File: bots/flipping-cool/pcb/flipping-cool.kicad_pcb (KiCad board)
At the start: 2 copper layers, 90 x 70 mm, 71 parts, among them J1 XT30_BATTERY_IN_GNB4502S80AHV, J10 MATEK_ELRS_R24_P6_PWM, J11 R24_P6_VBAT_TELEMETRY_SENSE, J2 REMOVABLE_LINK_OR_RATED_SWITCH, J20 WEKA_POWER_INPUT_XT30, J21 WEKA_PWM_INPUTS_NAMED, J22 WEKA_MOTOR_OUTPUT_SOLDER_PADS, J23 MOTOR_FRONT_LEFT_POLOLU_3064, J24 MOTOR_REAR_LEFT_POLOLU_3064, J25 MOTOR_FRONT_RIGHT_POLOLU_3064, J26 MOTOR_REAR_RIGHT_POLOLU_3064, J3 VISIBLE_POWER_LED_CURRENT_LIM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, J30 SAVOX_SH0255MGP_FRONT_REAR_AX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, J31 SAVOX_SH0255MGP_LEFT_RIGHT_AX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, J32 SPARE_SERVO_PWM5, J33 SPARE_SERVO_PWM6, J4 2S_BALANCE_SENSE_NO_CHARGE, J40 SPARE_SWITCHED_VBAT_OUT_FUSED, J41 SPARE_6V_ACCESSORY, J42 OPTIONAL_CRSF_UART_PADS, J43 PWM_SPARE_BREAKOUT, J44 PIT_DEBUG_POWER_COMMS, J45 OPTIONAL_POLOLU_D24V5F3_3V3, J46 FUTURE_MCU_POWER_COMMS, J47 FUTURE_MCU_PWM_I2C_TAPS, J48 FUTURE_MCU_ADC_LED, J49 I2C_SENSOR_STEMMA_QT_QWIIC, J5 POLOLU_D36V50F6_6V_5P5A_BEC, J50 COMMON_ANODE_RGB_STATUS_LED

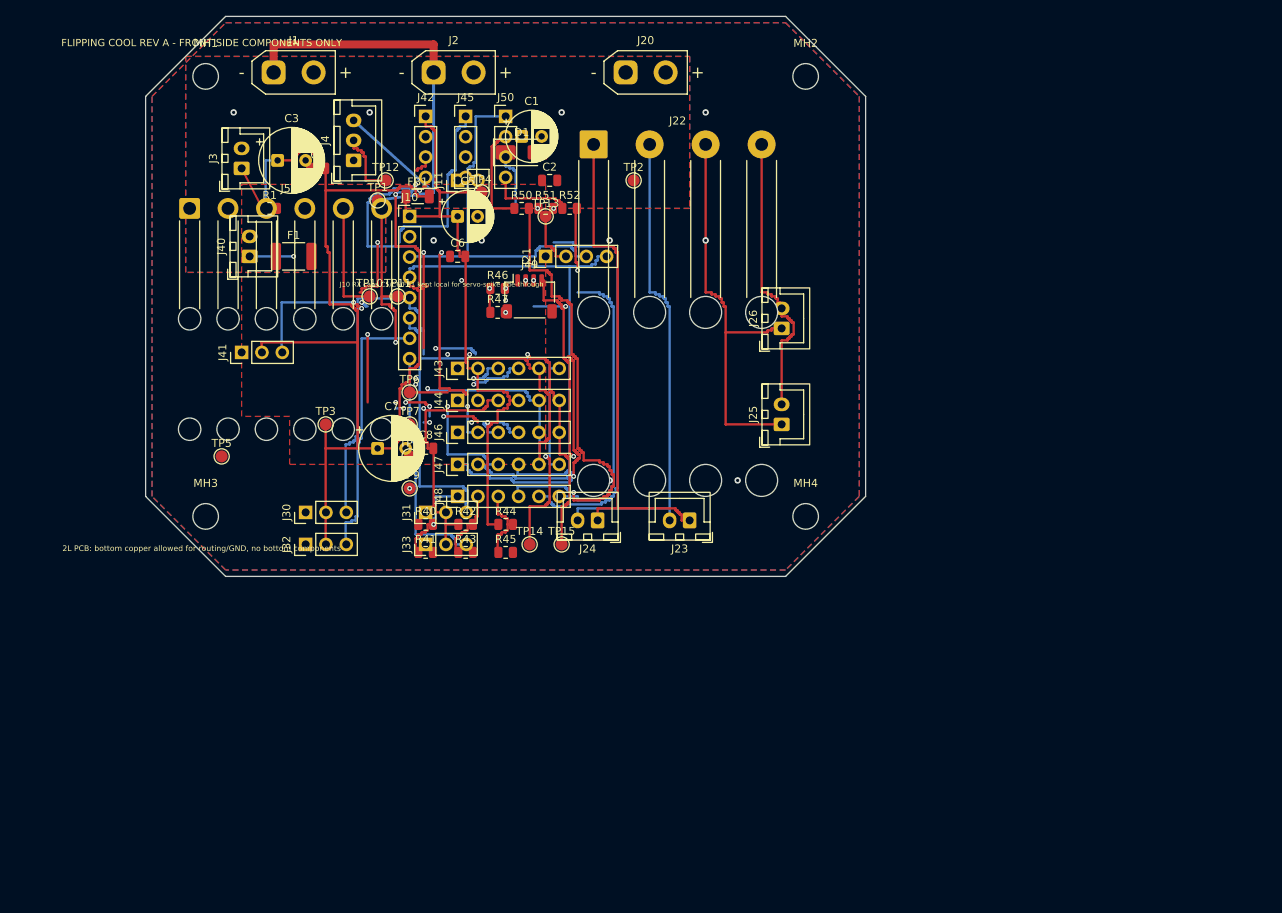
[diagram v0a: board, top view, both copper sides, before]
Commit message: Refactor KiCad PCB design by reorganizing net connections, adding a new mounting hole footprint, and updating existing footprints for resistors and test points. Adjust design rules in the project configuration, including hole clearance and via dimensions, to enhance layout precision and flexibility.
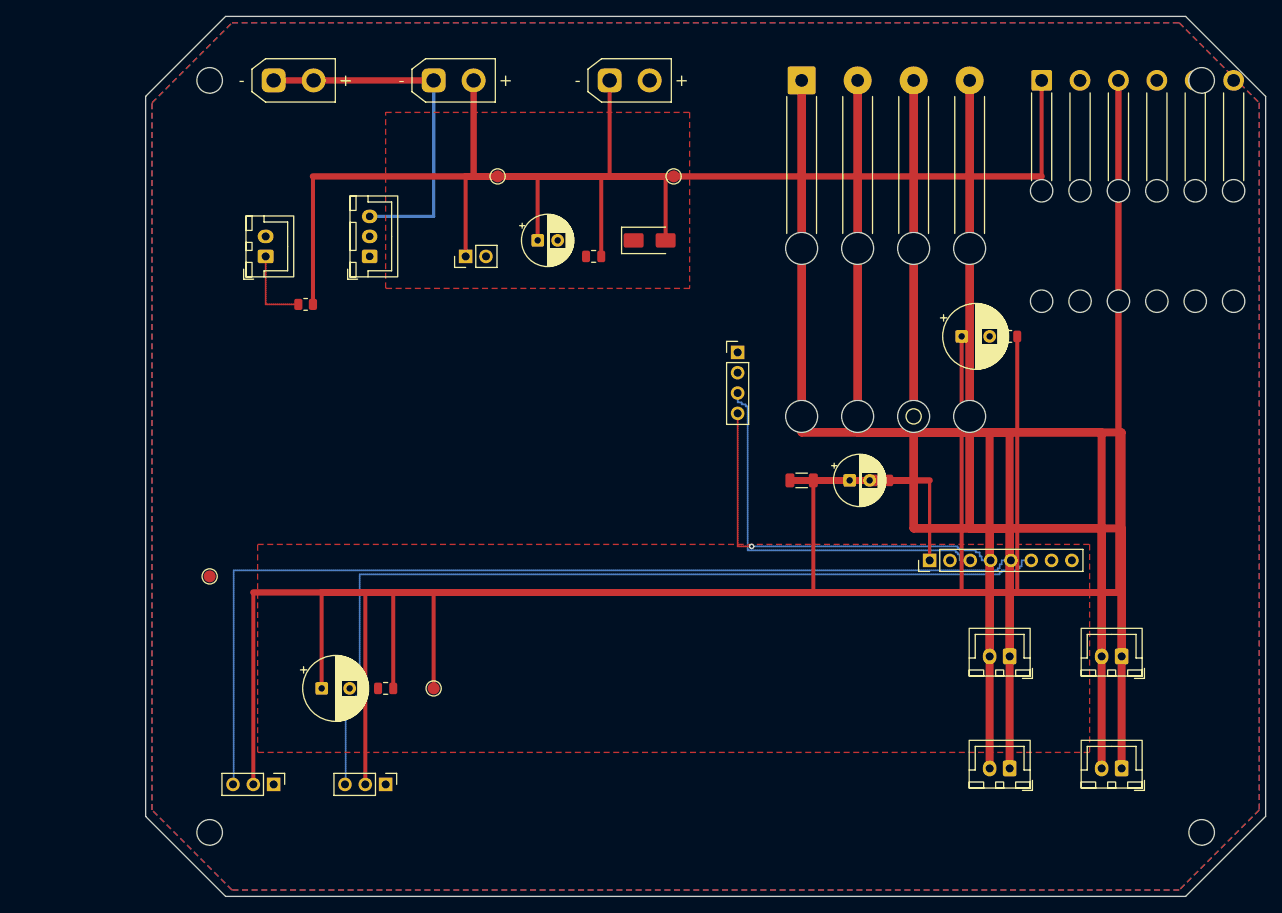
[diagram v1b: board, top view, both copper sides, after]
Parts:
- removed F1: MF-MSMF050_500mA_PTC, Fuse_1812_4532Metric_Pad1.30x3.40mm_HandSolder
- removed J32: SPARE_SERVO_PWM5, PinHeader_1x03_P2.54mm_Vertical
- removed J33: SPARE_SERVO_PWM6, PinHeader_1x03_P2.54mm_Vertical
- removed J40: SPARE_SWITCHED_VBAT_OUT_FUSED, JST_XH_B2B-XH-A_1x02_P2.50mm_Vertical
- removed J41: SPARE_6V_ACCESSORY, PinHeader_1x03_P2.54mm_Vertical
- removed J42: OPTIONAL_CRSF_UART_PADS, PinHeader_1x04_P2.54mm_Vertical
- removed J43: PWM_SPARE_BREAKOUT, PinHeader_1x06_P2.54mm_Vertical
- removed J44: PIT_DEBUG_POWER_COMMS, PinHeader_1x06_P2.54mm_Vertical
- removed J45: OPTIONAL_POLOLU_D24V5F3_3V3, PinHeader_1x04_P2.54mm_Vertical
- removed J46: FUTURE_MCU_POWER_COMMS, PinHeader_1x06_P2.54mm_Vertical
- removed J47: FUTURE_MCU_PWM_I2C_TAPS, PinHeader_1x06_P2.54mm_Vertical
- removed J48: FUTURE_MCU_ADC_LED, PinHeader_1x06_P2.54mm_Vertical
- removed J49: I2C_SENSOR_STEMMA_QT_QWIIC, JST_SH_SM04B-SRSS-TB_1x04-1MP_P1.00mm_Horizontal
- removed J50: COMMON_ANODE_RGB_STATUS_LED, PinHeader_1x04_P2.54mm_Vertical
- removed R40: 100k_ADC_VBAT_HI, R_0805_2012Metric
- removed R41: 47k_ADC_VBAT_LO, R_0805_2012Metric
- removed R42: 100k_ADC_SERVO_HI, R_0805_2012Metric
- removed R43: 47k_ADC_SERVO_LO, R_0805_2012Metric
- removed R44: 100k_ADC_RX_HI, R_0805_2012Metric
- removed R45: 47k_ADC_RX_LO, R_0805_2012Metric
- removed R46: 4k7_DNP_I2C_SDA_PULLUP, R_0805_2012Metric
- removed R47: 4k7_DNP_I2C_SCL_PULLUP, R_0805_2012Metric
- removed R50: 330R_STATUS_RED, R_0805_2012Metric
- removed R51: 330R_STATUS_GREEN, R_0805_2012Metric
- removed R52: 330R_STATUS_BLUE, R_0805_2012Metric
- removed TP10: BEC_EN_TP, TestPoint_Pad_D1.5mm
- removed TP11: BEC_PG_TP, TestPoint_Pad_D1.5mm
- removed TP12: CELL1_SENSE_TP, TestPoint_Pad_D1.5mm
- removed TP13: WEKA_5V_NC_TP, TestPoint_Pad_D1.5mm
- removed TP14: CRSF_TX_TP, TestPoint_Pad_D1.5mm
- removed TP15: CRSF_RX_TP, TestPoint_Pad_D1.5mm
- removed TP6: PWM_DRIVE_LEFT_TP, TestPoint_Pad_D1.5mm
- removed TP7: PWM_DRIVE_RIGHT_TP, TestPoint_Pad_D1.5mm
- removed TP8: PWM_WEAPON_FR_TP, TestPoint_Pad_D1.5mm
- removed TP9: PWM_WEAPON_LR_TP, TestPoint_Pad_D1.5mm
- moved J5 107.7 mm to (112.0, 8.00)
- moved C4 89.0 mm to (108.0, 40.0)
- moved C3 88.3 mm to (102.0, 40.0)
- moved J10 77.9 mm to (98.0, 68.0), turned to 90 degrees
- moved MH4 63.3 mm to (132.0, 102.0)
- moved J23 62.3 mm to (122.0, 94.0)
- moved TP4 60.8 mm to (96.0, 50.0)
- moved J24 60.1 mm to (108.0, 94.0)
- moved C6 59.9 mm to (92.0, 58.0)
- moved FB1 59.7 mm to (82.0, 58.0)
- moved C5 59.1 mm to (88.0, 58.0)
- moved J25 51.5 mm to (122.0, 80.0), turned to 180 degrees
- moved J26 49.9 mm to (108.0, 80.0), turned to 180 degrees
- moved MH2 49.5 mm to (132.0, 8.00)
- moved MH3 39.5 mm to (8.00, 102.0)
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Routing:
- net SERVO_6V: track 144.0 -> 774.5 mm
- net VBAT_SW: track 0.00 -> 270.0 mm
- net WEKA_M1A: track 63.0 -> 238.0 mm
- net WEKA_M1B: track 62.5 -> 219.0 mm
- net WEKA_M2A: track 52.0 -> 182.0 mm, vias 1 -> 0
- net WEKA_M2B: track 38.0 -> 163.0 mm
- net CRSF_TX: track 65.0 -> 0.00 mm, vias 4 -> 0
- net CRSF_RX: track 63.2 -> 0.00 mm, vias 4 -> 0
- net STATUS_LED_R_N: track 61.5 -> 0.00 mm, vias 1 -> 0
- net PWM_WEAPON_FR: track 68.8 -> 125.2 mm, vias 2 -> 0
- net AUX_3V3_SHDN: track 56.5 -> 0.00 mm, vias 8 -> 0
- net PWM_SPARE_5: track 54.5 -> 0.00 mm, vias 4 -> 0
- net STATUS_LED_G_N: track 52.0 -> 0.00 mm, vias 1 -> 0
- net AUX_3V3: track 51.0 -> 0.00 mm, vias 6 -> 0
- net PWM_WEAPON_LR: track 63.8 -> 113.8 mm, vias 1 -> 0
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- removed copper zone on B.Cu, net VBAT_SW
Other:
- board size 90 x 70 mm -> 140 x 110 mm
- board text removed: "2L PCB: bottom copper allowed for routing/GND, no bottom components"
- board text removed: "FLIPPING COOL REV A - FRONT SIDE COMPONENTS ONLY"
- board text removed: "J10 RX caps C5/C6/FB1 kept local for servo-spike ride-through"

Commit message: Update KiCad PCB design by renaming footprints for resistors, capacitors, connectors, and test points to include component categories. Adjust footprint positions for improved layout accuracy and consistency across the design.
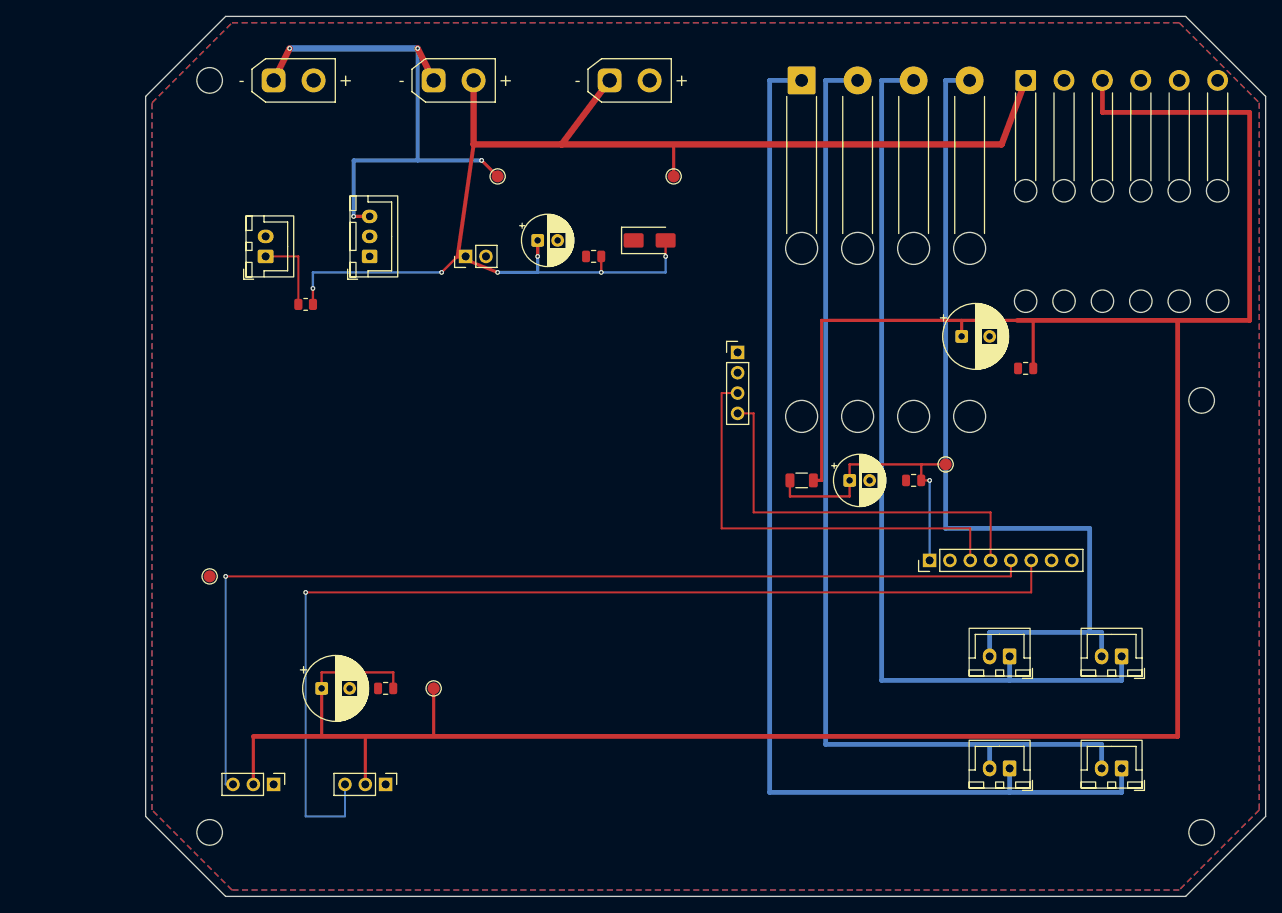
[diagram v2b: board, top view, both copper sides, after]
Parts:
- C1, C5: footprint CP_Radial_D6.3mm_P2.50mm -> Capacitor_THT:CP_Radial_D6.3mm_P2.50mm
- C2, C4, C6, C8: footprint C_0805_2012Metric -> Capacitor_SMD:C_0805_2012Metric
- C3, C7: footprint CP_Radial_D8.0mm_P3.50mm -> Capacitor_THT:CP_Radial_D8.0mm_P3.50mm
- D1: footprint D_SMA -> Diode_SMD:D_SMA
- FB1: footprint R_1206_3216Metric -> Resistor_SMD:R_1206_3216Metric
- J1: footprint AMASS_XT30UPB-M_1x02_P5.0mm_Vertical -> Connector_AMASS:AMASS_XT30UPB-M_1x02_P5.0mm_Vertical
- J10: footprint PinHeader_1x08_P2.54mm_Vertical -> Connector_PinHeader_2.54mm:PinHeader_1x08_P2.54mm_Vertical
- J11: footprint PinHeader_1x02_P2.54mm_Vertical -> Connector_PinHeader_2.54mm:PinHeader_1x02_P2.54mm_Vertical
- J2, J20: footprint AMASS_XT30UPB-F_1x02_P5.0mm_Vertical -> Connector_AMASS:AMASS_XT30UPB-F_1x02_P5.0mm_Vertical
- J21: footprint PinHeader_1x04_P2.54mm_Vertical -> Connector_PinHeader_2.54mm:PinHeader_1x04_P2.54mm_Vertical
- J22: footprint SolderWire-0.75sqmm_1x04_P7mm_D1.25mm_OD3.5mm_Relief2x -> Connector_Wire:SolderWire-0.75sqmm_1x04_P7mm_D1.25mm_OD3.5mm_Relief2x
- J23, J24, J25, J26, J3: footprint JST_XH_B2B-XH-A_1x02_P2.50mm_Vertical -> Connector_JST:JST_XH_B2B-XH-A_1x02_P2.50mm_Vertical
- J30, J31: footprint PinHeader_1x03_P2.54mm_Vertical -> Connector_PinHeader_2.54mm:PinHeader_1x03_P2.54mm_Vertical
- J4: footprint JST_XH_B3B-XH-A_1x03_P2.50mm_Vertical -> Connector_JST:JST_XH_B3B-XH-A_1x03_P2.50mm_Vertical
- J5: footprint SolderWire-0.75sqmm_1x06_P4.8mm_D1.25mm_OD2.3mm_Relief2x -> Connector_Wire:SolderWire-0.75sqmm_1x06_P4.8mm_D1.25mm_OD2.3mm_Relief2x
- R1: footprint R_0805_2012Metric -> Resistor_SMD:R_0805_2012Metric
- TP1, TP2, TP3, TP4, TP5: footprint TestPoint_Pad_D1.5mm -> TestPoint:TestPoint_Pad_D1.5mm
- moved MH2 40.0 mm to (132.0, 48.0)
- moved TP4 7.21 mm to (100.0, 56.0)
- moved C4 4.47 mm to (110.0, 44.0)
- moved C6 4.00 mm to (96.0, 58.0)
- moved J5 2.00 mm to (110.0, 8.00)
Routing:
- net SERVO_6V: track 774.5 -> 335.4 mm
- net VBAT_SW: track 270.0 -> 173.0 mm, vias 0 -> 6
- net WEKA_M1A: track 238.0 -> 143.0 mm
- net WEKA_M1B: track 219.0 -> 127.5 mm
- net WEKA_M2A: track 182.0 -> 115.0 mm
- net WEKA_M2B: track 163.0 -> 110.0 mm
- net RX_6V: track 70.8 -> 38.5 mm, vias 0 -> 1
- net PWM_WEAPON_LR: track 113.8 -> 131.6 mm, vias 0 -> 1
- net PWM_DRIVE_LEFT: track 50.0 -> 54.0 mm
- net PWM_WEAPON_FR: track 125.2 -> 127.1 mm, vias 0 -> 1
- net VBAT_RAW: track 65.0 -> 66.8 mm, vias 0 -> 4
- net PWM_DRIVE_RIGHT: vias 1 -> 0
- removed copper zone on F.Cu, net SERVO_6V
- removed copper zone on F.Cu, net VBAT_SW
